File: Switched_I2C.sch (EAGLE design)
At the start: 14 parts, among them Q1 MOSFET-NCH-DMG3404L

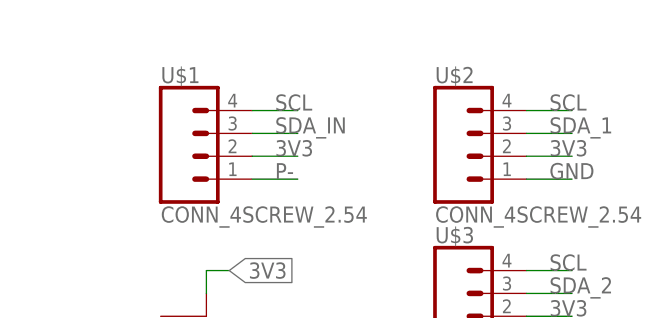
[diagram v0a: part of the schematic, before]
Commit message: Fixed silk screen issues on Switched_I2C board
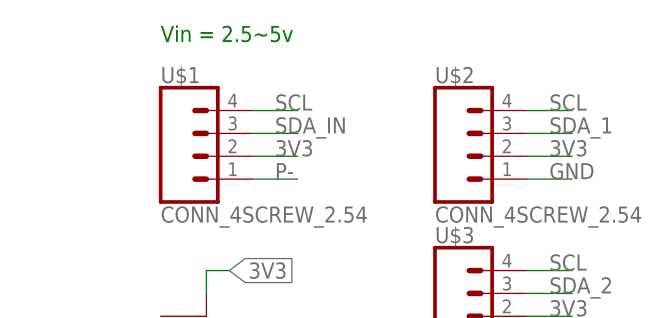
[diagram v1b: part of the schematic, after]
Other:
- note added: "Vin = 2.5~5v"
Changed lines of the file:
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@@
 <sheet>
 <plain>
+<text x="5.08" y="83.82" size="1.778" layer="91">Vin = 2.5~5v</text>
 </plain>
 <instances>
